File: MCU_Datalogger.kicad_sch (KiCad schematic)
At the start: 1 part

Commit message: add all component
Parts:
- removed U?: ATmega328P-P, Package_DIP:DIP-28_W7.62mm, symbol MCU_Microchip_ATmega:ATmega328P-P
- added BT?: Battery, symbol Device:Battery
- added C? (x4): C, symbol Device:C
- added C?: C_Polarized, symbol Device:C_Polarized
- added D? (x2): LED, symbol Device:LED
- added H? (x4): MountingHole, symbol Mechanical:MountingHole
- added R? (x7): R, symbol Device:R
- added U?: ATMEGA328P-AU, ATMEGA328P-AU:QFP80P900X900X120-32N, symbol ATMEGA328P-AU:ATMEGA328P-AU
- added U? (x2): 24LC1025, symbol Memory_EEPROM:24LC1025
- added U?: DS1337S_, DS1337S_:SOIC127P600X175-8N, symbol DS1337S_:DS1337S_
- added Y? (x2): Crystal, symbol Device:Crystal
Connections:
- new net: U?.21 (GND), U?.3 (GND), U?.5 (GND)
- new net: U?.4 (VCC), U?.6 (VCC)
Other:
- added sheet Connectors (Connectors.kicad_sch)
- title: $(project_name) -> MCU Datalogger with memory and clock

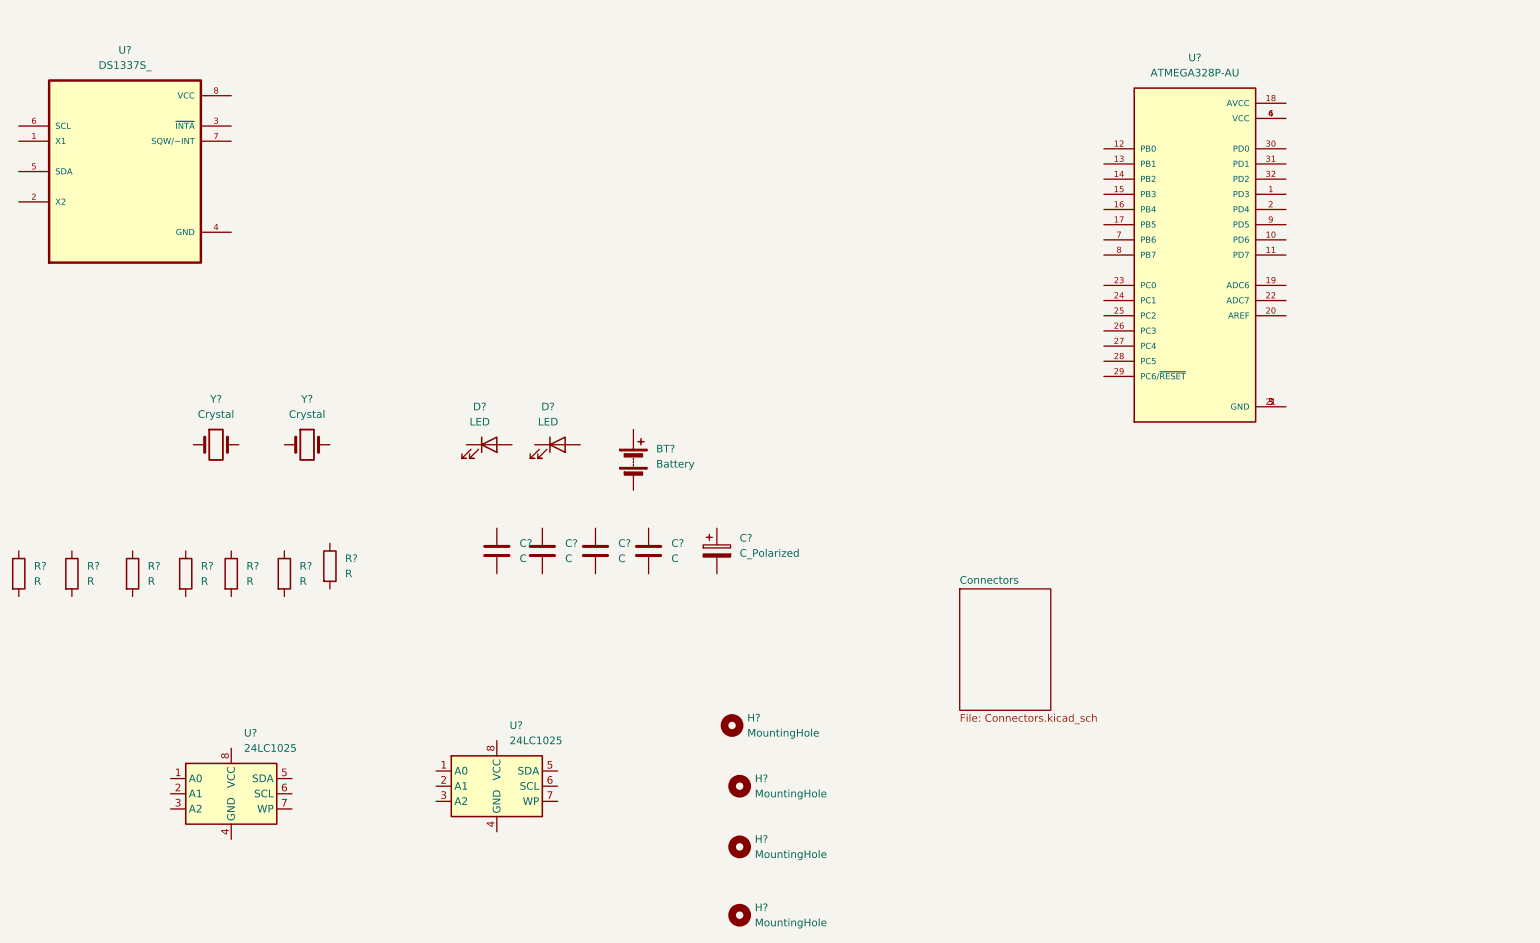
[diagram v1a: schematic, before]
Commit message: change the location of symbols(arrange) and annotate
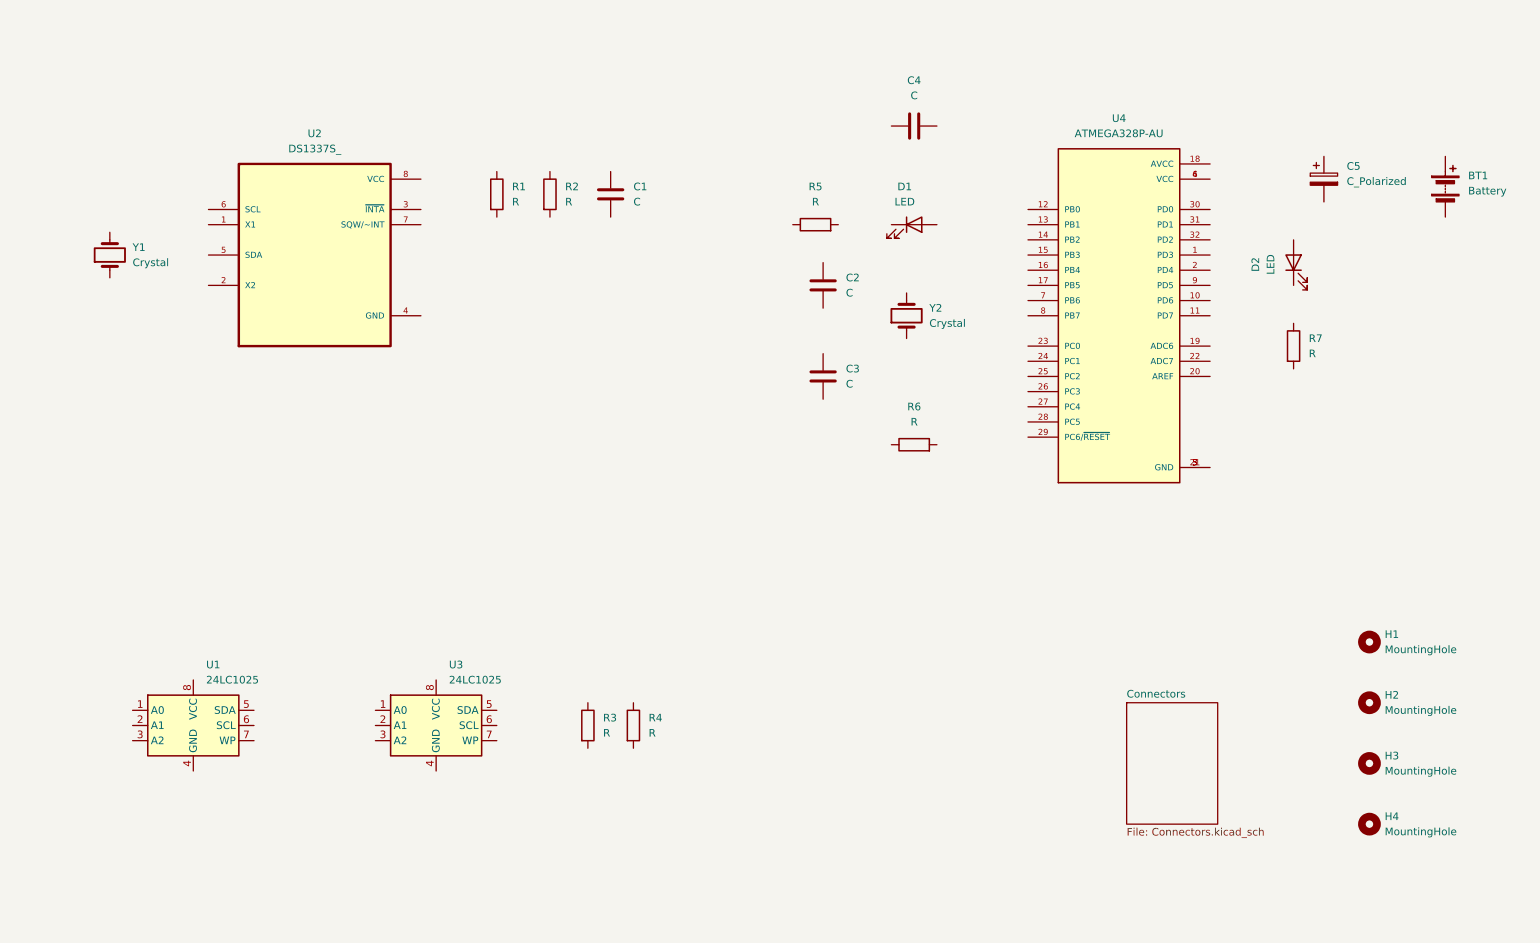
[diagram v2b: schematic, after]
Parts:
- gave numbers to parts that had none: 25
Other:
- moved on the sheet: BT1, C1, C2, C3, C4, C5, D1, D2, H1, H2, H3, H4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

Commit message: update symbol value
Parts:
- C1, C4: value C -> 0.1uf
- C2, C3: value C -> 22pF
- C5: value C_Polarized -> 100nF
- R1, R2, R6: value R -> 10K
- R3, R4: value R -> 4.7K
- R5, R7: value R -> 330
- Y1: value Crystal -> 32.768 KHz
- Y2: value Crystal -> 16MHz
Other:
- moved on the sheet: R4
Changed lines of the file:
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@@
 			)
 		)
-		(property "Value" "R"
+		(property "Value" "330"
 			(at 161.29 52.07 90)
 			(effects
@@
 			)
 		)
+		(property "Purpose" ""
+			(at 161.29 55.88 0)
+			(effects
+				(font
+					(size 1.27 1.27)
+				)
+			)
+		)
 		(pin "1"
 		)
@@
 			)
 		)
-		(property "Value" "C"
+		(property "Value" "22pF"
 			(at 166.37 82.5499 0)
 			(effects
@@
 			)
 		)
+		(property "Purpose" ""
+			(at 162.56 81.28 0)
+			(effects
+				(font
+					(size 1.27 1.27)
+				)
+			)
+		)
 		(pin "1"
 		)
@@
 			)
 		)
-		(property "Value" "R"
+		(property "Value" "4.7K"
 			(at 125.73 140.9699 0)
 			(effects
@@
 			)
 		)
+		(property "Purpose" ""
+			(at 123.19 139.7 0)
+			(effects
+				(font
+					(size 1.27 1.27)
+				)
+			)
+		)
 		(pin "1"
 		)
@@
 			)
 		)
-		(property "Value" "Crystal"
+		(property "Value" "16MHz"
 			(at 180.34 72.3899 90)
 			(effects
@@
 			)
 		)
+		(property "Purpose" ""
+			(at 176.53 71.12 0)
+			(effects
+				(font
+					(size 1.27 1.27)
+				)
+			)
+		)
 		(pin "1"
 		)
@@
 			)
 		)
-		(property "Value" "C"
+		(property "Value" "0.1uf"
 			(at 177.8 34.29 90)
 			(effects
@@
 			)
 		)
+		(property "Purpose" ""
+			(at 177.8 39.37 0)
+			(effects
+				(font
+					(size 1.27 1.27)
+				)
+			)
+		)
 		(pin "1"
 		)
@@
 			)
 		)
-		(property "Value" "R"
+		(property "Value" "10K"
 			(at 177.8 88.9 90)
 			(effects
@@
 			)
 		)
+		(property "Purpose" ""
+			(at 177.8 92.71 0)
+			(effects
+				(font
+					(size 1.27 1.27)
+				)
+			)
+		)
 		(pin "1"
 		)
@@
 			)
 		)
-		(property "Value" "R"
+		(property "Value" "330"
 			(at 243.84 77.4699 0)
 			(effects
@@
 			)
 		)
+		(property "Purpose" ""
+			(at 241.3 76.2 0)
+			(effects
+				(font
+					(size 1.27 1.27)
+				)
+			)
+		)
 		(pin "1"
 		)
@@
 			)
 		)
-		(property "Value" "C"
+		(property "Value" "22pF"
 			(at 166.37 67.3099 0)
 			(effects
@@
 			)
 		)
+		(property "Purpose" ""
+			(at 162.56 66.04 0)
+			(effects
+				(font
+					(size 1.27 1.27)
+				)
+			)
+		)
 		(pin "1"
 		)
@@
 			)
 		)
-		(property "Value" "C_Polarized"
+		(property "Value" "100nF"
 			(at 250.19 48.6409 0)
 			(effects
@@
 			)
 		)
+		(property "Purpose" ""
+			(at 246.38 48.26 0)
+			(effects
+				(font
+					(size 1.27 1.27)
+				)
+			)
+		)
 		(pin "2"
 		)
@@
 			)
 		)
-		(property "Value" "R"
+		(property "Value" "10K"
 			(at 119.38 52.0699 0)
 			(effects
@@
 			)
 		)
+		(property "Purpose" ""
+			(at 116.84 50.8 0)
+			(effects
+				(font
+					(size 1.27 1.27)
+				)
+			)
+		)
 		(pin "1"
 		)
@@
 			)
 		)
-		(property "Value" "Crystal"
+		(property "Value" "32.768 KHz"
 			(at 46.99 62.2299 90)
 			(effects
@@
 			)
 		)
+		(property "Purpose" ""
+			(at 43.18 60.96 0)
+			(effects
+				(font
+					(size 1.27 1.27)
+				)
+			)
+		)
 		(pin "1"
 		)
@@
 			)
 		)
-		(property "Value" "R"
+		(property "Value" "10K"
 			(at 110.49 52.0699 0)
 			(effects
@@
 			)
 		)
+		(property "Purpose" ""
+			(at 107.95 50.8 0)
+			(effects
+				(font
+					(size 1.27 1.27)
+				)
+			)
+		)
 		(pin "1"
 		)
@@
 			)
 		)
-		(property "Value" "C"
+		(property "Value" "0.1uf"
 			(at 130.81 52.0699 0)
 			(effects
@@
 			)
 		)
+		(property "Purpose" ""
+			(at 127 50.8 0)
+			(effects
+				(font
+					(size 1.27 1.27)
+				)
+			)
+		)
 		(pin "1"
 		)
@@
 	(symbol
 		(lib_id "Device:R")
-		(at 130.81 139.7 0)
+		(at 132.08 139.7 0)
 		(unit 1)
 		(exclude_from_sim no)
@@
 		(fields_autoplaced yes)
 		(property "Reference" "R4"
-			(at 133.35 138.4299 0)
-			(effects
-				(font
-					(size 1.27 1.27)
-				)
-				(justify left)
-			)
-		)
-		(property "Value" "R"
-			(at 133.35 140.9699 0)
-			(effects
-				(font
-					(size 1.27 1.27)
-				)
-				(justify left)
-			)
-		)
-		(property "Footprint" ""
-			(at 129.032 139.7 90)
+			(at 134.62 138.4299 0)
+			(effects
+				(font
+					(size 1.27 1.27)
+				)
+				(justify left)
+			)
+		)
+		(property "Value" "4.7K"
+			(at 134.62 140.9699 0)
+			(effects
+				(font
+					(size 1.27 1.27)
+				)
+				(justify left)
+			)
+		)
+		(property "Footprint" ""
+			(at 130.302 139.7 90)
 			(effects
 				(font
@@
 		)
 		(property "Datasheet" "~"
-			(at 130.81 139.7 0)
+			(at 132.08 139.7 0)
 			(effects
 				(font
@@
 		)
 		(property "Description" "Resistor"
-			(at 130.81 139.7 0)
-			(effects
-				(font
-					(size 1.27 1.27)
-				)
-				(hide yes)
-			)
-		)
+			(at 132.08 139.7 0)
+			(effects
+				(font
+					(size 1.27 1.27)
+				)
+				(hide yes)
+			)
+		)
+		(property "Purpose" ""
+			(at 132.08 139.7 0)
+			(effects
+				(font
+					(size 1.27 1.27)
+				)
+			)
+		)

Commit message: completed symbol-footprint assignment
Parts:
- BT1: footprint (none) -> Connector_PinHeader_2.54mm:PinHeader_1x02_P2.54mm_Vertical
- C1, C2, C3, C4, C5: footprint (none) -> Capacitor_SMD:C_0805_2012Metric
- D1, D2: footprint (none) -> LED_SMD:LED_0805_2012Metric
- H1, H2, H3, H4: footprint (none) -> MountingHole:MountingHole_2.1mm
- R1, R2, R3, R4, R5, R6, R7: footprint (none) -> Resistor_SMD:R_0805_2012Metric
- U1, U3: footprint (none) -> Package_SO:SOIC-8_5.3x5.3mm_P1.27mm
- U2: footprint DS1337S_:SOIC127P600X175-8N -> Footprints:SOIC127P600X175-8N
- U4: footprint ATMEGA328P-AU:QFP80P900X900X120-32N -> Footprints:QFP80P900X900X120-32N
- Y1, Y2: footprint (none) -> Crystal:Crystal_SMD_5032-2Pin_5.0x3.2mm_HandSoldering
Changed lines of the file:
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@@
 			)
 		)
-		(property "Footprint" ""
+		(property "Footprint" "LED_SMD:LED_0805_2012Metric"
 			(at 177.8 55.88 0)
 			(effects
@@
 			)
 		)
-		(property "Footprint" ""
+		(property "Footprint" "Resistor_SMD:R_0805_2012Metric"
 			(at 161.29 57.658 90)
 			(effects
@@
 			)
 		)
-		(property "Footprint" ""
+		(property "Footprint" "Capacitor_SMD:C_0805_2012Metric"
 			(at 163.5252 85.09 0)
 			(effects
@@
 			)
 		)
-		(property "Footprint" ""
+		(property "Footprint" "Resistor_SMD:R_0805_2012Metric"
 			(at 121.412 139.7 90)
 			(effects
@@
 			)
 		)
-		(property "Footprint" ""
+		(property "Footprint" "MountingHole:MountingHole_2.1mm"
 			(at 254 135.89 0)
 			(effects
@@
 			)
 		)
-		(property "Footprint" ""
+		(property "Footprint" "Crystal:Crystal_SMD_5032-2Pin_5.0x3.2mm_HandSoldering"
 			(at 176.53 71.12 0)
 			(effects
@@
 			)
 		)
-		(property "Footprint" ""
+		(property "Footprint" "Capacitor_SMD:C_0805_2012Metric"
 			(at 181.61 38.4048 0)
 			(effects
@@
 			)
 		)
-		(property "Footprint" ""
+		(property "Footprint" "Resistor_SMD:R_0805_2012Metric"
 			(at 177.8 94.488 90)
 			(effects
@@
 			)
 		)
-		(property "Footprint" ""
+		(property "Footprint" "Resistor_SMD:R_0805_2012Metric"
 			(at 239.522 76.2 90)
 			(effects
@@
 			)
 		)
-		(property "Footprint" ""
+		(property "Footprint" "Capacitor_SMD:C_0805_2012Metric"
 			(at 163.5252 69.85 0)
 			(effects
@@
 			)
 		)
-		(property "Footprint" "ATMEGA328P-AU:QFP80P900X900X120-32N"
+		(property "Footprint" "Footprints:QFP80P900X900X120-32N"
 			(at 212.09 71.12 0)
 			(effects
@@
 			)
 		)
-		(property "Footprint" ""
+		(property "Footprint" "Connector_PinHeader_2.54mm:PinHeader_1x02_P2.54mm_Vertical"
 			(at 266.7 48.006 90)
 			(effects
@@
 			)
 		)
-		(property "Footprint" ""
+		(property "Footprint" "Package_SO:SOIC-8_5.3x5.3mm_P1.27mm"
 			(at 57.15 139.7 0)
 			(effects
@@
 			)
 		)
-		(property "Footprint" ""
+		(property "Footprint" "Capacitor_SMD:C_0805_2012Metric"
 			(at 247.3452 52.07 0)
 			(effects
@@
 			)
 		)
-		(property "Footprint" ""
+		(property "Footprint" "MountingHole:MountingHole_2.1mm"
 			(at 254 125.73 0)
 			(effects
@@
 			)
 		)
-		(property "Footprint" ""
+		(property "Footprint" "Resistor_SMD:R_0805_2012Metric"
 			(at 115.062 50.8 90)
 			(effects
@@
 			)
 		)
-		(property "Footprint" ""
+		(property "Footprint" "Package_SO:SOIC-8_5.3x5.3mm_P1.27mm"
 			(at 97.79 139.7 0)
 			(effects
@@
 			)
 		)
-		(property "Footprint" "DS1337S_:SOIC127P600X175-8N"
+		(property "Footprint" "Footprints:SOIC127P600X175-8N"
 			(at 77.47 60.96 0)
 			(effects
@@
 			)
 		)
-		(property "Footprint" ""
+		(property "Footprint" "Crystal:Crystal_SMD_5032-2Pin_5.0x3.2mm_HandSoldering"
 			(at 43.18 60.96 0)
 			(effects
@@
 			)
 		)
-		(property "Footprint" ""
+		(property "Footprint" "LED_SMD:LED_0805_2012Metric"
 			(at 241.3 62.23 0)
 			(effects
@@
 			)
 		)
-		(property "Footprint" ""
+		(property "Footprint" "Resistor_SMD:R_0805_2012Metric"
 			(at 106.172 50.8 90)
 			(effects
@@
 			)
 		)
-		(property "Footprint" ""
+		(property "Footprint" "MountingHole:MountingHole_2.1mm"
 			(at 254 146.05 0)
 			(effects
@@
 			)
 		)
-		(property "Footprint" ""
+		(property "Footprint" "MountingHole:MountingHole_2.1mm"
 			(at 254 156.21 0)
 			(effects
@@
 			)
 		)
-		(property "Footprint" ""
+		(property "Footprint" "Capacitor_SMD:C_0805_2012Metric"
 			(at 127.9652 54.61 0)
 			(effects
@@
 			)
 		)
-		(property "Footprint" ""
+		(property "Footprint" "Resistor_SMD:R_0805_2012Metric"
 			(at 130.302 139.7 90)
 			(effects

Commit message: Completed Sch wiring
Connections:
- net at D1.1 (K): now also R5.2
- net SCL: now reaches D1.2 (A)
- net SCL: now also R3.2, U1.6 (SCL), U2.6 (SCL), U3.6 (SCL), U4.17 (PB5), U4.28 (PC5)
- net GND: now reaches R5.1
- net GND: now also BT1.2 (-), C1.2, C2.1, C3.1, C4.1, C5.2, R7.2, U1.4 (GND), U1.7 (WP), U2.4 (GND), U3.2 (A1), U3.4 (GND), U3.7 (WP), U4.21 (GND), U4.3 (GND), U4.5 (GND)
- net at C3.2: now also U4.8 (PB7), Y2.1
- net Vcc: now reaches R3.1
- net Vcc: now also R4.1, R6.1, U1.1 (A0), U1.2 (A1), U1.3 (A2), U1.8 (VCC), U3.1 (A0), U3.3 (A2), U3.8 (VCC)
- net at Y2.2: now also C2.2, U4.7 (PB6)
- net at C4.2: now also U4.20 (AREF)
- net RESET: now reaches R6.2
- net RESET: now also U4.29 (PC6/~{RESET})
- net at R7.1: now also D2.1 (K)
- net D3: now reaches U4.1 (PD3)
- net D6: now reaches U4.10 (PD6)
- net D7: now reaches U4.11 (PD7)
- net D8: now reaches U4.12 (PB0)
- net MOSI: now reaches U4.15 (PB3)
- net MISO: now reaches U4.16 (PB4)
- net at U4.18 (AVCC): now also BT1.1 (+), C5.1, D2.2 (A), U4.4 (VCC), U4.6 (VCC)
- net D4: now reaches U4.2 (PD4)
- net SDA: now reaches U4.27 (PC4)
- net SDA: now also R4.2, U1.5 (SDA), U2.5 (SDA), U3.5 (SDA)
- net RX: now reaches U4.30 (PD0)
- net TX: now reaches U4.31 (PD1)
- net D2: now reaches U4.32 (PD2)
- net D5: now reaches U4.9 (PD5)
- net at R2.1: now also C1.1, R1.1, U2.8 (VCC)
- net at R2.2: now also U2.7 (SQW/~INT)
- net at U2.1 (X1): now also Y1.2
- net at U2.2 (X2): now also Y1.1
- net at U2.3 (~{INTA}): now also R1.2
- no-connect marks 0 -> 8
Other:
- moved on the sheet: BT1, C2, C3, C4, C5, D1, D2, R3, R4, R5, R6, R7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
